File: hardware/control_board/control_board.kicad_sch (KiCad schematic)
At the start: 0 parts

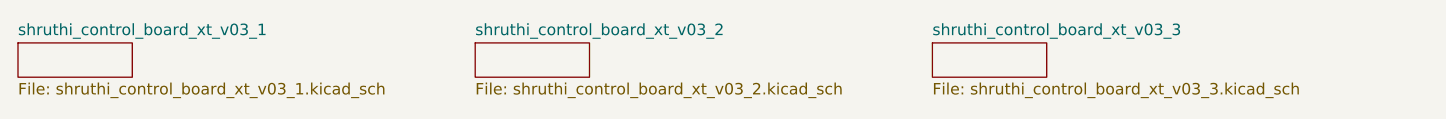
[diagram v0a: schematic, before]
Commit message: rename sheets
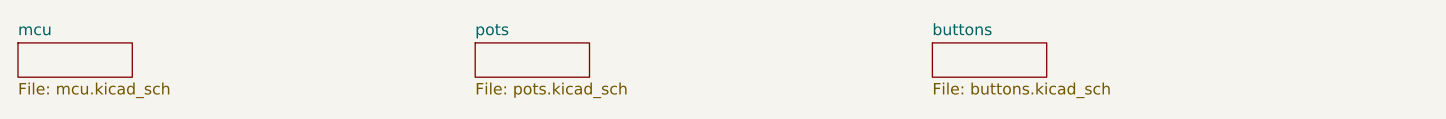
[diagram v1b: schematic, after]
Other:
- sheet shruthi_control_board_xt_v03_1 renamed mcu
- sheet shruthi_control_board_xt_v03_2 renamed pots
- sheet shruthi_control_board_xt_v03_3 renamed buttons
- sheet buttons: file shruthi_control_board_xt_v03_3.kicad_sch -> buttons.kicad_sch
- sheet mcu: file shruthi_control_board_xt_v03_1.kicad_sch -> mcu.kicad_sch
- sheet pots: file shruthi_control_board_xt_v03_2.kicad_sch -> pots.kicad_sch
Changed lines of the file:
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@@
 			(color 0 0 0 0.0000)
 		)
-		(property "Sheetname" "shruthi_control_board_xt_v03_2"
+		(property "Sheetname" "pots"
 			(at 76.2 24.6884 0)
 			(effects
@@
 			)
 		)
-		(property "Sheetfile" "shruthi_control_board_xt_v03_2.kicad_sch"
+		(property "Sheetfile" "pots.kicad_sch"
 			(at 76.2 29.7946 0)
 			(effects
@@
 		)
 		(instances
-			(project "shruthi_control_board_xt_v03"
+			(project "control_board"
 				(path "/2c840835-6e01-4901-947c-222cae369ab9"
 					(page "2")
@@
 			(color 0 0 0 0.0000)
 		)
-		(property "Sheetname" "shruthi_control_board_xt_v03_3"
+		(property "Sheetname" "buttons"
 			(at 127 24.6884 0)
 			(effects
@@
 			)
 		)
-		(property "Sheetfile" "shruthi_control_board_xt_v03_3.kicad_sch"
+		(property "Sheetfile" "buttons.kicad_sch"
 			(at 127 29.7946 0)
 			(effects
@@
 		)
 		(instances
-			(project "shruthi_control_board_xt_v03"
+			(project "control_board"
 				(path "/2c840835-6e01-4901-947c-222cae369ab9"
 					(page "3")
@@
 			(color 0 0 0 0.0000)
 		)
-		(property "Sheetname" "shruthi_control_board_xt_v03_1"
+		(property "Sheetname" "mcu"
 			(at 25.4 24.6884 0)
 			(effects
@@
 			)
 		)
-		(property "Sheetfile" "shruthi_control_board_xt_v03_1.kicad_sch"
+		(property "Sheetfile" "mcu.kicad_sch"
 			(at 25.4 29.7946 0)
 			(effects
@@
 		)
 		(instances
-			(project "shruthi_control_board_xt_v03"
+			(project "control_board"
 				(path "/2c840835-6e01-4901-947c-222cae369ab9"
 					(page "1")

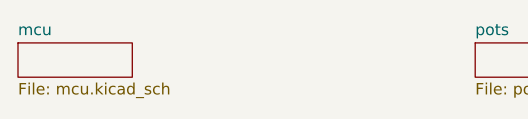
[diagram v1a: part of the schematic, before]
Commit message: move all logic components to daughterboard, move MIDI to new board
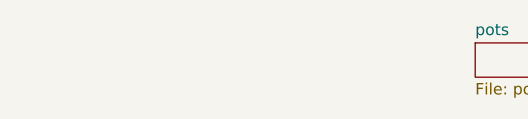
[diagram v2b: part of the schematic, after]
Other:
- removed sheet mcu
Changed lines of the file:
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@@
-		)
-	)
-	(sheet
-		(at 25.4 25.4)
-		(size 12.7 3.81)
-		(exclude_from_sim no)
-		(in_bom yes)
-		(on_board yes)
-		(dnp no)
-		(fields_autoplaced yes)
-		(stroke
-			(width 0)
-			(type solid)
-		)
-		(fill
-			(color 0 0 0 0.0000)
-		)
-		(property "Sheetname" "mcu"
-			(at 25.4 24.6884 0)
-			(effects
-				(font
-					(size 1.27 1.27)
-				)
-				(justify left bottom)
-			)
-		)
-		(property "Sheetfile" "mcu.kicad_sch"
-			(at 25.4 29.7946 0)
-			(effects
-				(font
-					(size 1.27 1.27)
-				)
-				(justify left top)
-			)
-		)
-		(instances
-			(project "control_board"
-				(path "/2c840835-6e01-4901-947c-222cae369ab9"
-					(page "1")
-				)
-			)
 		)
 	)
